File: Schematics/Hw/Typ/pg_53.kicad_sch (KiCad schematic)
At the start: 6 parts, among them U5501 93S48, U5502 93S48, U5503 93S48, U5504 F86, U5505 F86, U5506 93S48

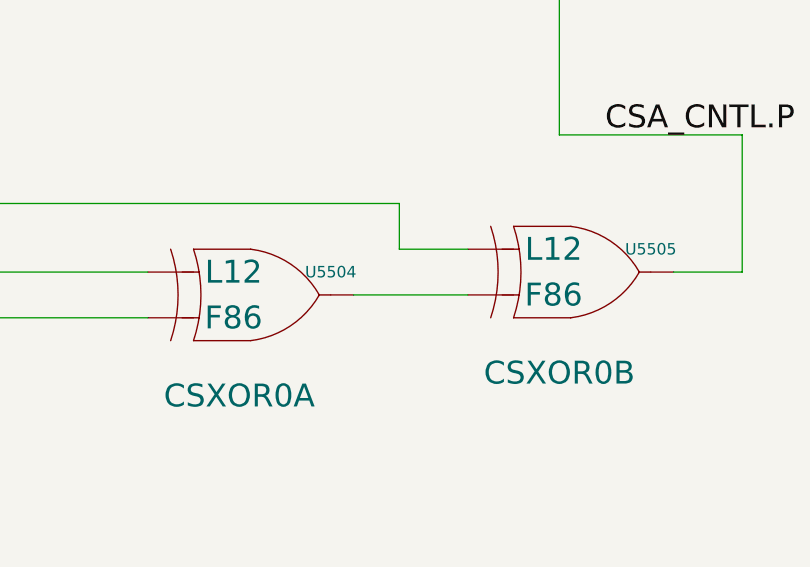
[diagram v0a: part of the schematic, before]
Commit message: Upgrade to KiCad9
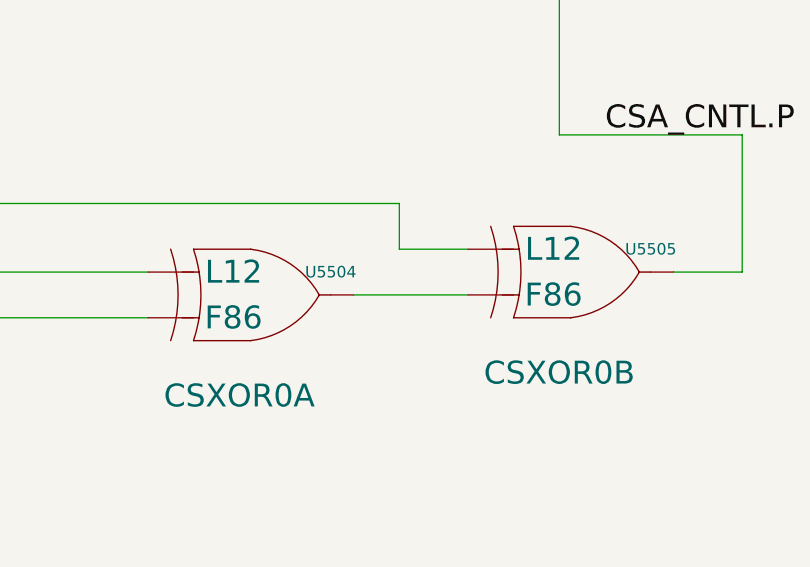
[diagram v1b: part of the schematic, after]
